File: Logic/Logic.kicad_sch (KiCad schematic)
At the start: 6 parts, among them J1 Conn_01x04_Pin

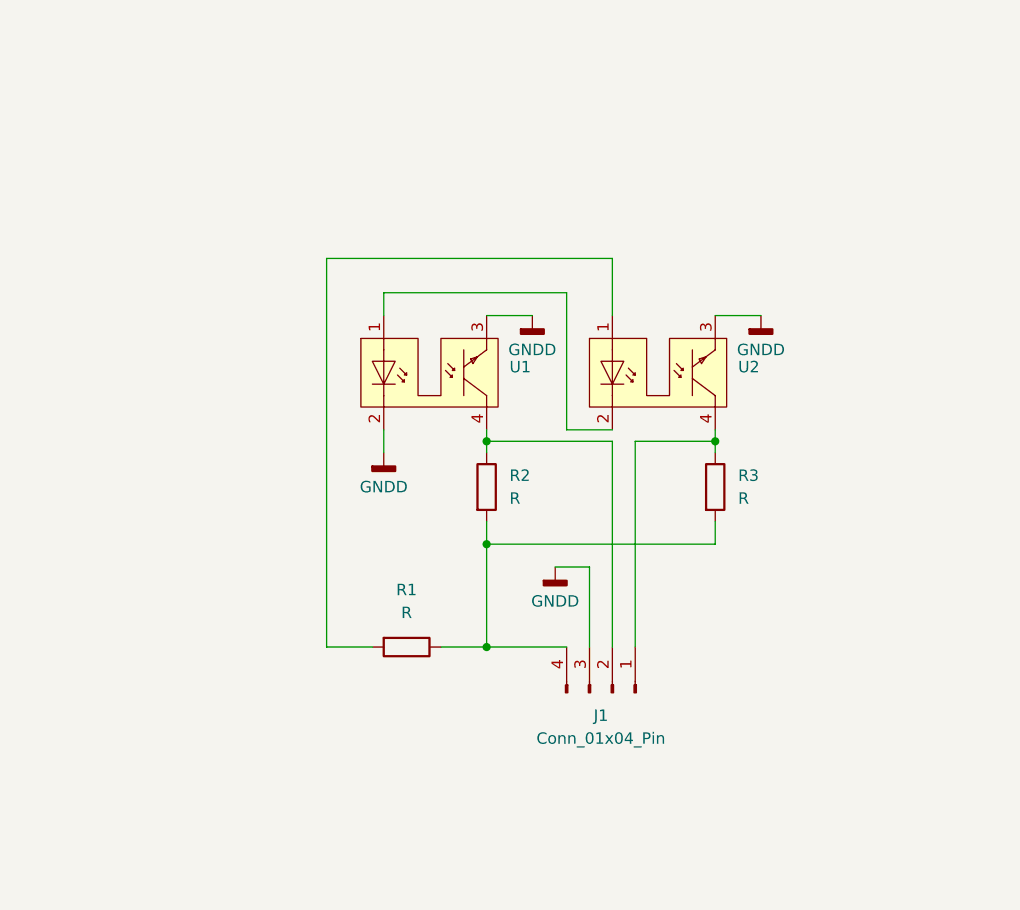
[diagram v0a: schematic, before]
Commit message: Add Schmitt-Trigger and Datasheets
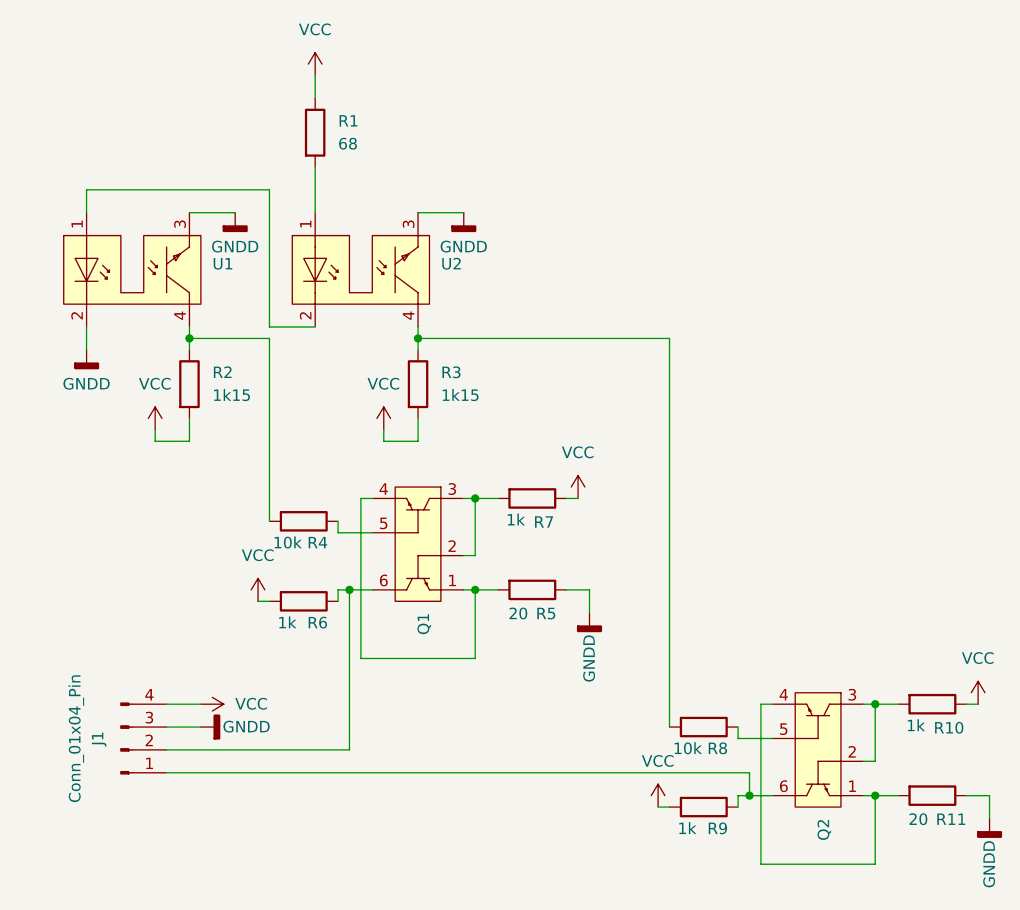
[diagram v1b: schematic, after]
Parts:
- added Q1, Q2: ~, Package_TO_SOT_SMD:SOT-363_SC-70-6, symbol External_Parts:MBT3904DW1T1
- added R10, R6, R7, R9: 1k, Resistor_SMD:R_1210_3225Metric_Pad1.30x2.65mm_HandSolder, symbol Device:R
- added R11, R5: 20, Resistor_SMD:R_1210_3225Metric_Pad1.30x2.65mm_HandSolder, symbol Device:R
- added R4, R8: 10k, Resistor_SMD:R_1210_3225Metric_Pad1.30x2.65mm_HandSolder, symbol Device:R
- R1: value R -> 68
- R2, R3: value R -> 1k15
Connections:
- net GNDD: now also R11.1, R5.1
- net at R3.1, U2.4: now also R8.2; no longer J1.1 (Pin_1)
- net at R2.1, U1.4: now also R4.2; no longer J1.2 (Pin_2)
- net VCC: now reaches J1.4 (Pin_4), R1.1, R2.2, R3.2
- net VCC: now also R10.1, R6.2, R7.1, R9.2
- new net: Q1.2, Q1.3, R7.2
- new net: J1.1 (Pin_1), Q2.6, R9.1
- new net: J1.2 (Pin_2), Q1.6, R6.1
- new net: Q2.1, Q2.4, R11.2
- new net: Q1.5, R4.1
- new net: Q2.2, Q2.3, R10.2
- new net: Q2.5, R8.1
- new net: Q1.1, Q1.4, R5.2
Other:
- moved on the sheet: J1, R1, R2, R3, U1, U2

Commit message: user save
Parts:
- R1, R10, R11, R2, R3, R4, R5, R6, R7, R8, R9: footprint Resistor_SMD:R_1210_3225Metric_Pad1.30x2.65mm_HandSolder -> Resistor_SMD:R_0603_1608Metric_Pad0.98x0.95mm_HandSolder
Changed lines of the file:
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@@
 			)
 		)
-		(property "Footprint" "Resistor_SMD:R_1210_3225Metric_Pad1.30x2.65mm_HandSolder"
+		(property "Footprint" "Resistor_SMD:R_0603_1608Metric_Pad0.98x0.95mm_HandSolder"
 			(at 142.24 94.742 90)
 			(effects
@@
 			)
 		)
-		(property "Footprint" "Resistor_SMD:R_1210_3225Metric_Pad1.30x2.65mm_HandSolder"
+		(property "Footprint" "Resistor_SMD:R_0603_1608Metric_Pad0.98x0.95mm_HandSolder"
 			(at 116.332 55.88 90)
 			(effects
@@
 			)
 		)
-		(property "Footprint" "Resistor_SMD:R_1210_3225Metric_Pad1.30x2.65mm_HandSolder"
+		(property "Footprint" "Resistor_SMD:R_0603_1608Metric_Pad0.98x0.95mm_HandSolder"
 			(at 186.69 127.762 90)
 			(effects
@@
 			)
 		)
-		(property "Footprint" "Resistor_SMD:R_1210_3225Metric_Pad1.30x2.65mm_HandSolder"
+		(property "Footprint" "Resistor_SMD:R_0603_1608Metric_Pad0.98x0.95mm_HandSolder"
 			(at 116.84 97.282 90)
 			(effects
@@
 			)
 		)
-		(property "Footprint" "Resistor_SMD:R_1210_3225Metric_Pad1.30x2.65mm_HandSolder"
+		(property "Footprint" "Resistor_SMD:R_0603_1608Metric_Pad0.98x0.95mm_HandSolder"
 			(at 161.29 129.032 90)
 			(effects
@@
 			)
 		)
-		(property "Footprint" "Resistor_SMD:R_1210_3225Metric_Pad1.30x2.65mm_HandSolder"
+		(property "Footprint" "Resistor_SMD:R_0603_1608Metric_Pad0.98x0.95mm_HandSolder"
 			(at 142.24 104.902 90)
 			(effects
@@
 			)
 		)
-		(property "Footprint" "Resistor_SMD:R_1210_3225Metric_Pad1.30x2.65mm_HandSolder"
+		(property "Footprint" "Resistor_SMD:R_0603_1608Metric_Pad0.98x0.95mm_HandSolder"
 			(at 161.29 120.142 90)
 			(effects
@@
 			)
 		)
-		(property "Footprint" "Resistor_SMD:R_1210_3225Metric_Pad1.30x2.65mm_HandSolder"
+		(property "Footprint" "Resistor_SMD:R_0603_1608Metric_Pad0.98x0.95mm_HandSolder"
 			(at 127.762 83.82 90)
 			(effects
@@
 			)
 		)
-		(property "Footprint" "Resistor_SMD:R_1210_3225Metric_Pad1.30x2.65mm_HandSolder"
+		(property "Footprint" "Resistor_SMD:R_0603_1608Metric_Pad0.98x0.95mm_HandSolder"
 			(at 102.362 83.82 90)
 			(effects
@@
 			)
 		)
-		(property "Footprint" "Resistor_SMD:R_1210_3225Metric_Pad1.30x2.65mm_HandSolder"
+		(property "Footprint" "Resistor_SMD:R_0603_1608Metric_Pad0.98x0.95mm_HandSolder"
 			(at 186.69 117.602 90)
 			(effects
@@
 			)
 		)
-		(property "Footprint" "Resistor_SMD:R_1210_3225Metric_Pad1.30x2.65mm_HandSolder"
+		(property "Footprint" "Resistor_SMD:R_0603_1608Metric_Pad0.98x0.95mm_HandSolder"
 			(at 116.84 106.172 90)
 			(effects

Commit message: user save
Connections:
- net GNDD: now also R1.2; no longer U1.2
- net VCC: now also U1.1; no longer R1.1
- net at U2.1: now also U1.2; no longer R1.2
- net at U2.2: now also R1.1; no longer U1.1
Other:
- moved on the sheet: R1
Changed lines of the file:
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@@
+	(wire
+		(pts
+			(xy 118.11 77.47) (xy 118.11 80.01)
+		)
+		(stroke
+			(width 0)
+			(type default)
+		)
+	)
 	(wire
 		(pts
@@
 	(wire
 		(pts
+			(xy 92.71 63.5) (xy 92.71 64.77)
+		)
+		(stroke
+			(width 0)
+			(type default)
+		)
+	)
+	(wire
+		(pts
 			(xy 113.03 99.06) (xy 113.03 78.74)
 		)
@@
 	(wire
 		(pts
+			(xy 118.11 87.63) (xy 118.11 90.17)
+		)
+		(stroke
+			(width 0)
+			(type default)
+		)
+	)
+	(wire
+		(pts
 			(xy 129.54 78.74) (xy 157.48 78.74)
 		)
@@
 	(wire
 		(pts
+			(xy 85.09 55.88) (xy 118.11 55.88)
+		)
+		(stroke
+			(width 0)
+			(type default)
+		)
+	)
+	(wire
+		(pts
 			(xy 148.59 106.68) (xy 148.59 109.22)
 		)
@@
 	(wire
 		(pts
-			(xy 113.03 77.47) (xy 118.11 77.47)
-		)
-		(stroke
-			(width 0)
-			(type default)
-		)
-	)
-	(wire
-		(pts
 			(xy 101.6 124.46) (xy 121.92 124.46)
 		)
@@
 	(wire
 		(pts
+			(xy 92.71 81.28) (xy 85.09 81.28)
+		)
+		(stroke
+			(width 0)
+			(type default)
+		)
+	)
+	(wire
+		(pts
 			(xy 157.48 121.92) (xy 157.48 78.74)
 		)
@@
 	(wire
 		(pts
-			(xy 118.11 59.69) (xy 118.11 64.77)
-		)
-		(stroke
-			(width 0)
-			(type default)
-		)
-	)
-	(wire
-		(pts
-			(xy 92.71 77.47) (xy 92.71 80.01)
-		)
-		(stroke
-			(width 0)
-			(type default)
-		)
-	)
-	(wire
-		(pts
 			(xy 193.04 129.54) (xy 193.04 132.08)
 		)
@@
 	(wire
 		(pts
-			(xy 113.03 62.23) (xy 113.03 77.47)
-		)
-		(stroke
-			(width 0)
-			(type default)
-		)
-	)
-	(wire
-		(pts
 			(xy 129.54 78.74) (xy 129.54 80.01)
 		)
@@
 	(wire
 		(pts
-			(xy 118.11 49.53) (xy 118.11 52.07)
-		)
-		(stroke
-			(width 0)
-			(type default)
-		)
-	)
-	(wire
-		(pts
 			(xy 123.19 96.52) (xy 123.19 114.3)
 		)
@@
 	(wire
 		(pts
+			(xy 92.71 77.47) (xy 92.71 81.28)
+		)
+		(stroke
+			(width 0)
+			(type default)
+		)
+	)
+	(wire
+		(pts
 			(xy 120.65 107.95) (xy 120.65 106.68)
 		)
@@
 	(wire
 		(pts
+			(xy 85.09 81.28) (xy 85.09 55.88)
+		)
+		(stroke
+			(width 0)
+			(type default)
+		)
+	)
+	(wire
+		(pts
 			(xy 168.91 119.38) (xy 167.64 119.38)
 		)
@@
 	(wire
 		(pts
+			(xy 118.11 55.88) (xy 118.11 64.77)
+		)
+		(stroke
+			(width 0)
+			(type default)
+		)
+	)
+	(wire
+		(pts
 			(xy 121.92 124.46) (xy 121.92 106.68)
 		)
@@
 	(wire
 		(pts
-			(xy 92.71 62.23) (xy 113.03 62.23)
-		)
-		(stroke
-			(width 0)
-			(type default)
-		)
-	)
-	(wire
-		(pts
 			(xy 138.43 106.68) (xy 135.89 106.68)
 		)
@@
 		(pts
 			(xy 167.64 137.16) (xy 180.34 137.16)
-		)
-		(stroke
-			(width 0)
-			(type default)
-		)
-	)
-	(wire
-		(pts
-			(xy 92.71 64.77) (xy 92.71 62.23)
 		)
 		(stroke
@@
 	(symbol
 		(lib_id "Device:R")
-		(at 118.11 55.88 0)
+		(at 118.11 83.82 0)
 		(unit 1)
 		(exclude_from_sim no)
@@
 		(fields_autoplaced yes)
 		(property "Reference" "R1"
-			(at 120.65 54.6099 0)
+			(at 120.65 82.5499 0)
 			(effects
 				(font
@@
 		)
 		(property "Value" "68"
-			(at 120.65 57.1499 0)
+			(at 120.65 85.0899 0)
 			(effects
 				(font
@@
 		)
 		(property "Footprint" "Resistor_SMD:R_0603_1608Metric_Pad0.98x0.95mm_HandSolder"
-			(at 116.332 55.88 90)
+			(at 116.332 83.82 90)
 			(effects
 				(font
@@
 		)
 		(property "Datasheet" "~"
-			(at 118.11 55.88 0)
+			(at 118.11 83.82 0)
 			(effects
 				(font
@@
 		)
 		(property "Description" "Resistor"
-			(at 118.11 55.88 0)
+			(at 118.11 83.82 0)
 			(effects
 				(font
@@
 	(symbol
 		(lib_id "power:VCC")
-		(at 118.11 49.53 0)
+		(at 92.71 63.5 0)
 		(unit 1)
 		(exclude_from_sim no)
@@
 		(fields_autoplaced yes)
 		(property "Reference" "#PWR014"
-			(at 118.11 53.34 0)
+			(at 92.71 67.31 0)
 			(effects
 				(font
@@
 		)
 		(property "Value" "VCC"
-			(at 118.11 44.45 0)
+			(at 92.71 58.42 0)
 			(effects
 				(font
@@
 		)
 		(property "Footprint" ""
-			(at 118.11 49.53 0)
+			(at 92.71 63.5 0)
 			(effects
 				(font
@@
 		)
 		(property "Datasheet" ""
-			(at 118.11 49.53 0)
+			(at 92.71 63.5 0)
 			(effects
 				(font
@@
 		)
 		(property "Description" "Power symbol creates a global label with name \"VCC\""
-			(at 118.11 49.53 0)
+			(at 92.71 63.5 0)
 			(effects
 				(font
@@
 	(symbol
 		(lib_id "power:GNDD")
-		(at 92.71 80.01 0)
+		(at 118.11 90.17 0)
 		(unit 1)
 		(exclude_from_sim no)
@@
 		(fields_autoplaced yes)
 		(property "Reference" "#PWR03"
-			(at 92.71 86.36 0)
+			(at 118.11 96.52 0)
 			(effects
 				(font
@@
 		)
 		(property "Value" "GNDD"
-			(at 92.71 83.82 0)
+			(at 118.11 93.98 0)
 			(effects
 				(font
@@
 		)
 		(property "Footprint" ""
-			(at 92.71 80.01 0)
+			(at 118.11 90.17 0)
 			(effects
 				(font
@@
 		)
 		(property "Datasheet" ""
-			(at 92.71 80.01 0)
+			(at 118.11 90.17 0)
 			(effects
 				(font
@@
 		)
 		(property "Description" "Power symbol creates a global label with name \"GNDD\" , digital ground"
-			(at 92.71 80.01 0)
-			(effects
-				(font
+			(at 118.11 90.17 0)
+			(effects
+				(font
